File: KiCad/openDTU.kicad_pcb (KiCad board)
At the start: 4 copper layers, 40 x 50 mm, 53 parts, among them J1 USB_C_Receptacle_USB2.0, J2 Conn_Coaxial, J3 Micro_SD_Card, J4 Conn_02x05_Counter_Clockwise, Q1 BC817, Q2 BC817, SW1 SW_Push, SW2 SW_Push, U1 CH340C, U3 ESP32-WROOM-32, U4 nRF24L01P, U5 NCP1117-3.3_SOT223, Y1 Crystal

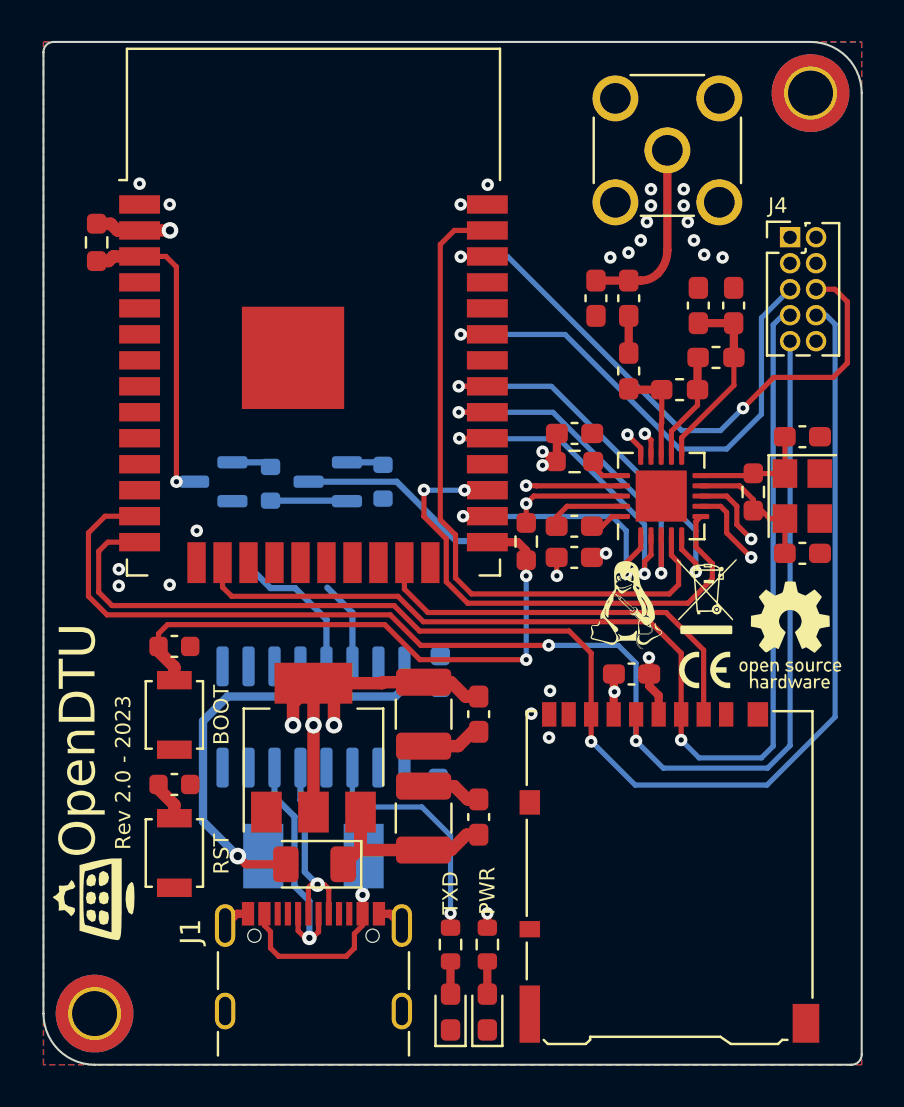
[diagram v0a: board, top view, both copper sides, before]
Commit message: all tracks first time routed
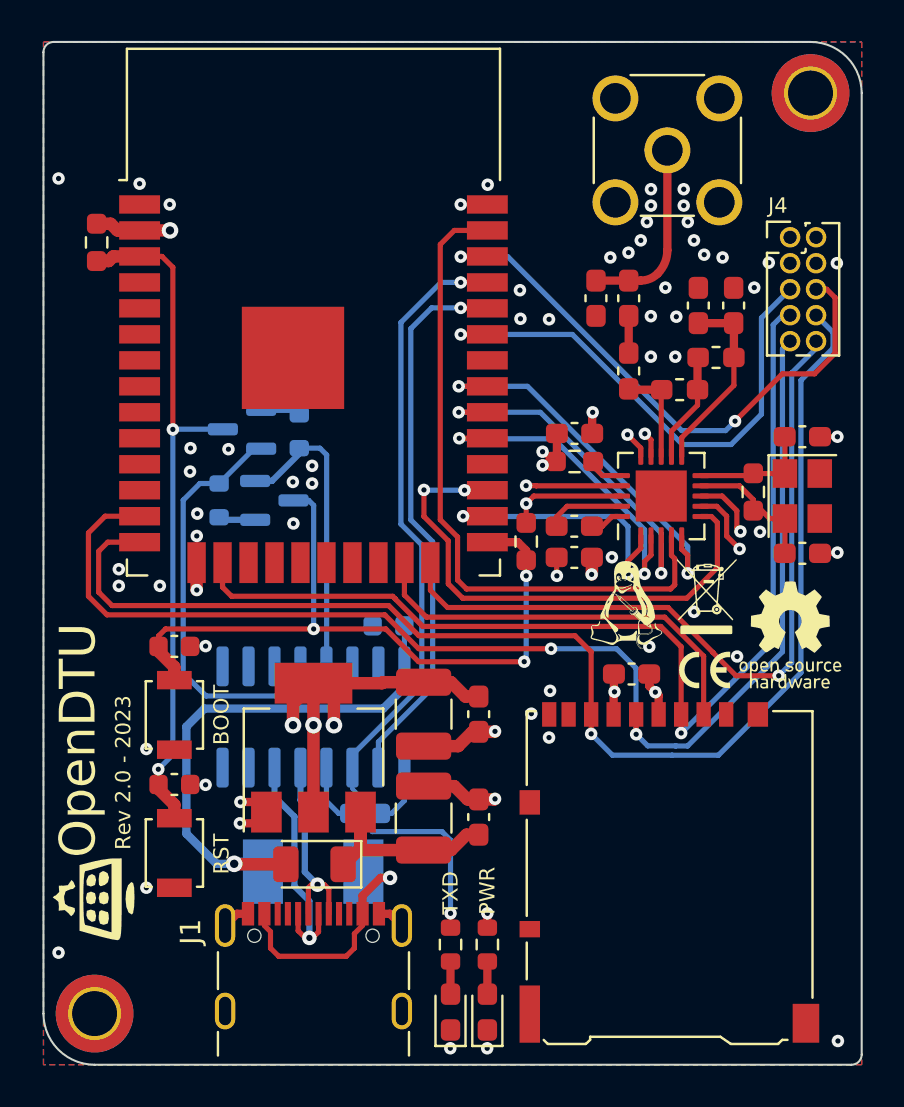
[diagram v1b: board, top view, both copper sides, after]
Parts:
- moved R5 8.06 mm to (134.1, 90.4), turned to -90 degrees
- moved C15 4.37 mm to (141.2, 105.7), turned to 0 degrees
- moved C16 3.39 mm to (142.4, 96.5), turned to 180 degrees
- moved Q1 2.93 mm to (135.2, 86.9)
- moved R4 2.93 mm to (138.0, 87.0)
- moved Q2 2.77 mm to (136.8, 90.4), turned to 0 degrees
- moved F1 0.76 mm to (138.7, 108.6)
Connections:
- J4 pad 10: unconnected-(J4-Pad10) -> /ESP.CS_EXT
- U3 pad 24: unconnected-(U3-Pad24) -> /ESP.CS_EXT
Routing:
- net /ESP.CS_EXT: track 0.00 -> 37.2 mm, vias 0 -> 1
- net /ESP.TXD: track 11.6 -> 40.4 mm, vias 1 -> 2
- net /ESP.RXD: track 0.00 -> 27.2 mm, vias 0 -> 1
- net Net-(Q1-Pad2): track 4.54 -> 23.2 mm
- net /ESP_EN: track 17.5 -> 34.0 mm, vias 1 -> 2
- net GND: track 22.1 -> 33.9 mm, vias 28 -> 69
- net /ESP.SCK_SD: track 67.5 -> 63.0 mm
- net Net-(Q2-Pad2): track 10.8 -> 14.8 mm
- net /ESP.MOSI_SD: track 55.9 -> 51.9 mm
- net /ESP.MISO_SD: track 68.3 -> 64.3 mm
- net Net-(C15-Pad1): track 0.00 -> 3.01 mm
- net /ESP.IO0: track 38.8 -> 35.8 mm, vias 2 -> 3
- net VBUS: track 25.4 -> 27.8 mm
- net +3.3V: track 42.1 -> 40.6 mm
- net /ESP.SCL: track 29.9 -> 28.5 mm
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
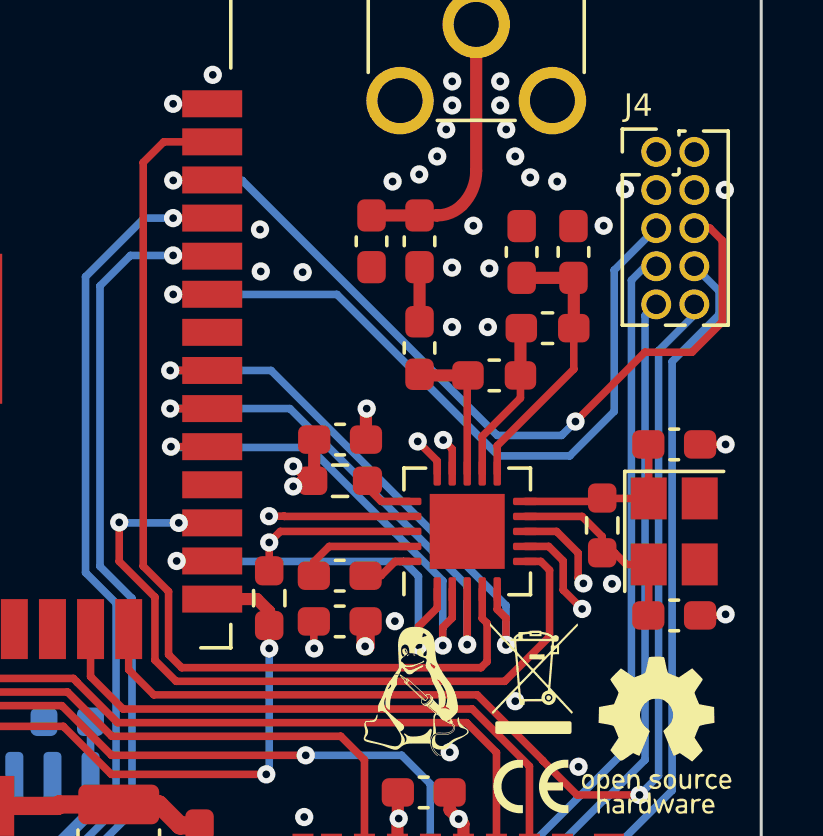
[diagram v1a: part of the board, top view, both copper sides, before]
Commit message: adding Frequency value to crystal an fixing crystal pin/footrpint assignment
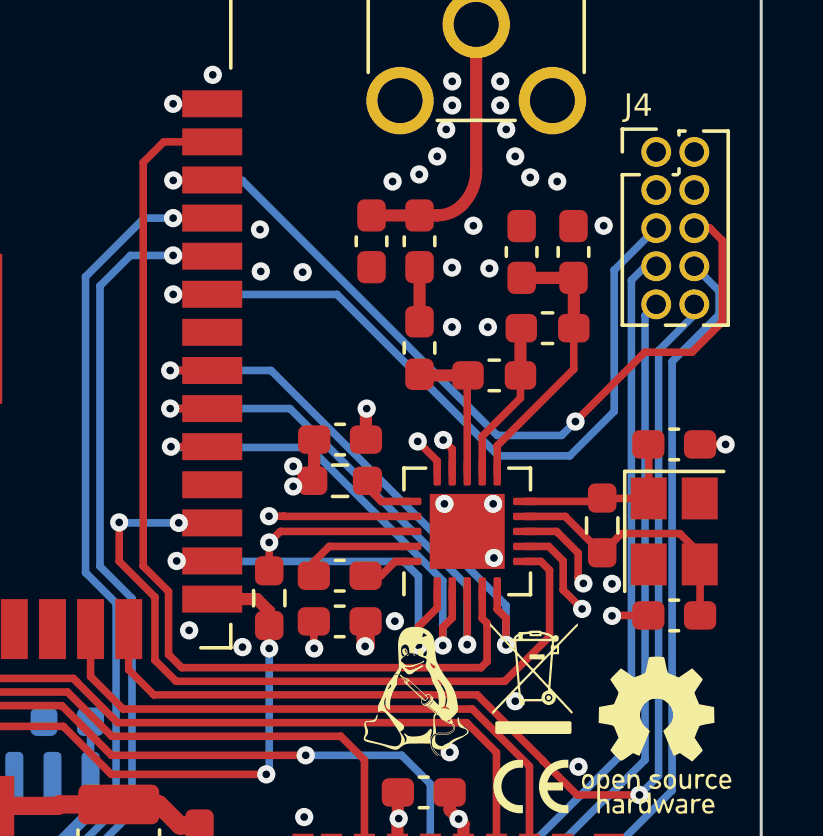
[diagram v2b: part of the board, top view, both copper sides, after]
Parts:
- C15, C16: value 100n -> 100nF
- Y1: value Crystal -> 16 MHz
- turned C5 to 180 degrees
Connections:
- Y1 pad 2: Net-(C5-Pad1) -> (no net)
- Y1 pad 3: (no net) -> Net-(C5-Pad1)
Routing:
- net Net-(C5-Pad1): track 6.80 -> 8.93 mm
- net GND: track 33.9 -> 34.3 mm, vias 69 -> 72

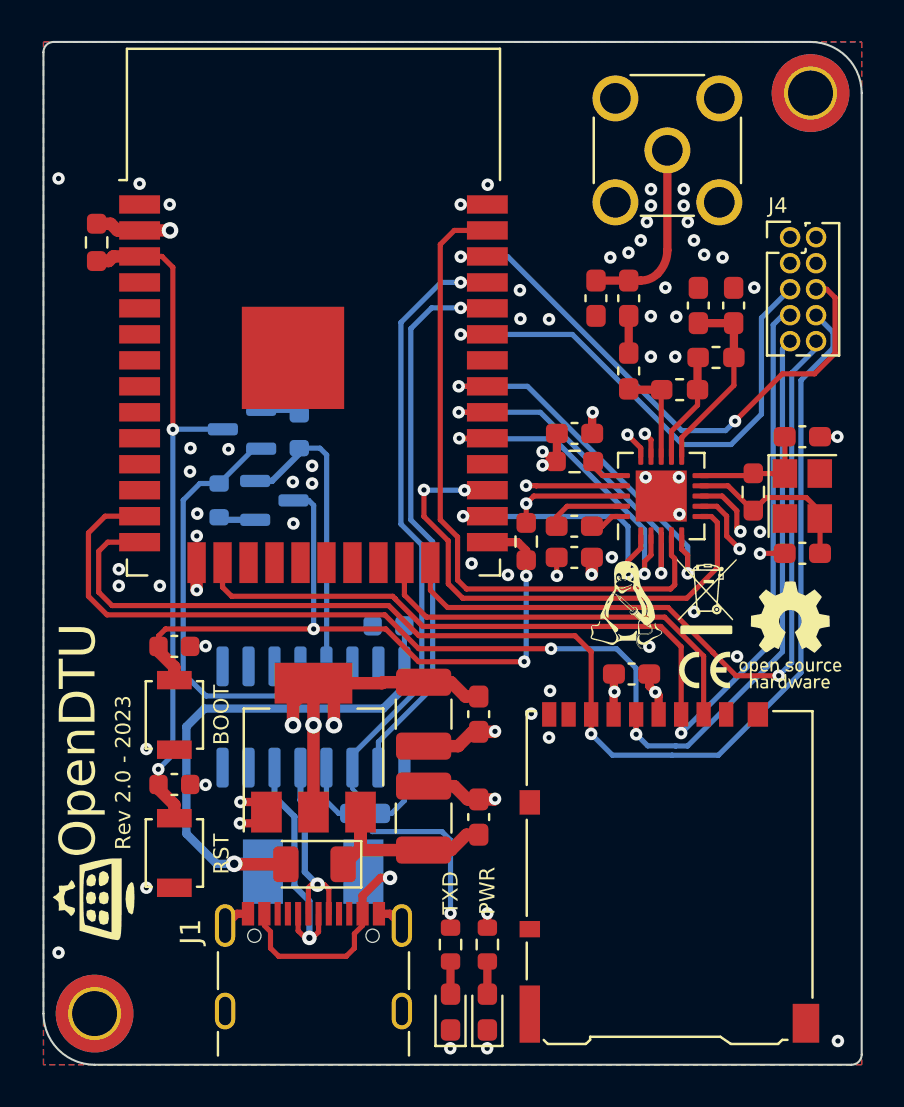
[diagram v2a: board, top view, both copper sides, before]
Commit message: adding 5k1 resistor for A5 and B5 of usb-c
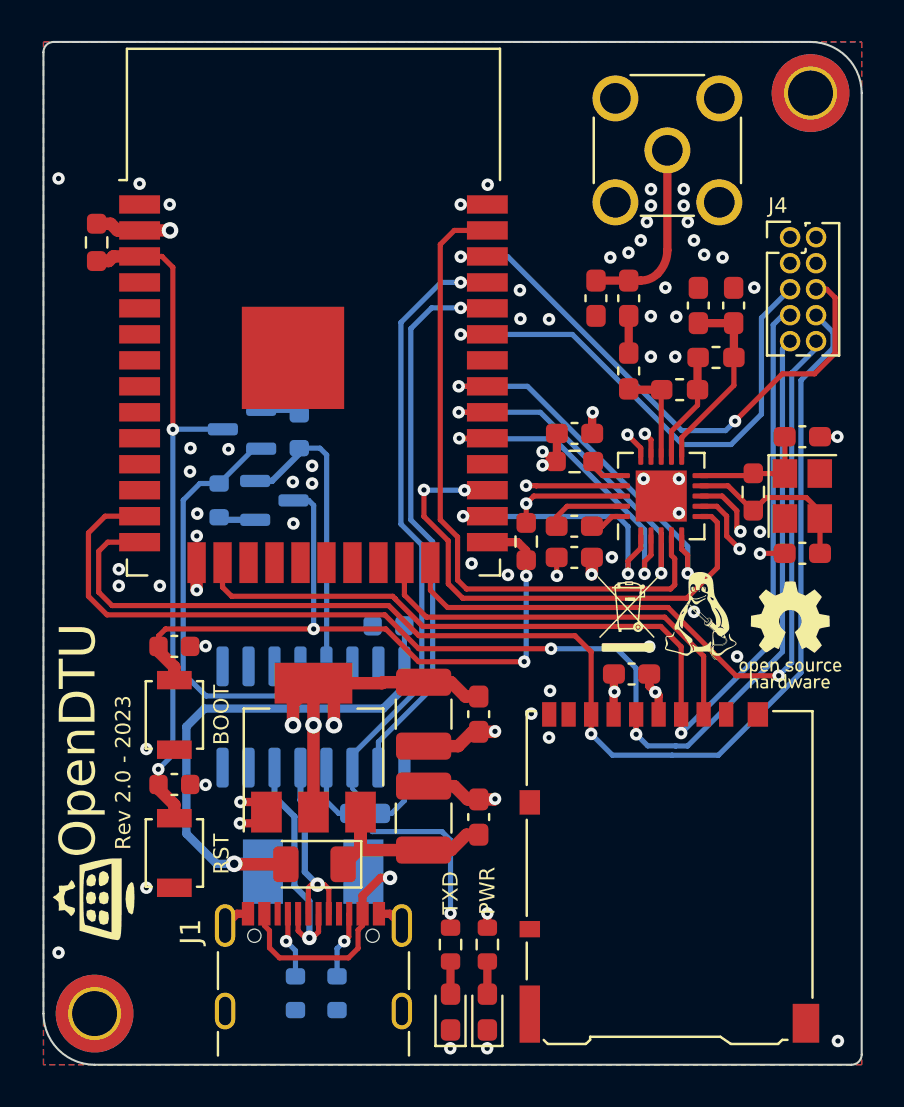
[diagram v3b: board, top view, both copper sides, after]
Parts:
- removed the G*** at (157.8, 98.7)
- added R10: 5k1, Resistor_SMD:R_0603_1608Metric, B.Cu at (137.8, 114.5)
- added R9: 5k1, Resistor_SMD:R_0603_1608Metric, B.Cu at (139.9, 114.5)
- moved G*** 3.94 mm to (154.2, 96.2)
- moved G*** 3.67 mm to (157.6, 95.3)
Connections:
- J1 pad A5: unconnected-(J1-PadA5) -> Net-(J1-PadA5)
- J1 pad B5: unconnected-(J1-PadB5) -> Net-(J1-PadB5)
- U4 pad 21: (no net) -> GND
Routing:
- net Net-(J1-PadB5): track 0.00 -> 3.31 mm, vias 0 -> 1
- net Net-(J1-PadA5): track 0.00 -> 3.28 mm, vias 0 -> 1

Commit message: update color of ESP32 wroom module
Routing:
- net +3.3V: track 40.6 -> 41.2 mm
- net GND: track 34.3 -> 34.9 mm
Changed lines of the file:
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@@
       (layer "F.SilkS" (type "Top Silk Screen") (color "White"))
       (layer "F.Paste" (type "Top Solder Paste"))
-      (layer "F.Mask" (type "Top Solder Mask") (color "Blue") (thickness 0.01))
+      (layer "F.Mask" (type "Top Solder Mask") (color "Black") (thickness 0.01))
       (layer "F.Cu" (type "copper") (thickness 0.035))
       (layer "dielectric 1" (type "prepreg") (thickness 0.14) (material "FR4") (epsilon_r 4.5) (loss_tangent 0.02))
@@
       (layer "dielectric 3" (type "prepreg") (thickness 0.14) (material "FR4") (epsilon_r 4.5) (loss_tangent 0.02))
       (layer "B.Cu" (type "copper") (thickness 0.035))
-      (layer "B.Mask" (type "Bottom Solder Mask") (color "Blue") (thickness 0.01))
+      (layer "B.Mask" (type "Bottom Solder Mask") (color "Black") (thickness 0.01))
       (layer "B.Paste" (type "Bottom Solder Paste"))
       (layer "B.SilkS" (type "Bottom Silk Screen") (color "White"))
@@
       )
     )
-    (model "${KICAD6_3DMODEL_DIR}/RF_Module.3dshapes/ESP32-WROOM-32.wrl"
+    (model "${KICAD6_3DMODEL_DIR}/RF_Module.3dshapes/ESP32-WROOM-32.wrl" hide
       (offset (xyz 0 0 0))
       (scale (xyz 1 1 1))
       (rotate (xyz 0 0 0))
     )
+    (model "${KIPRJMOD}/3D_Models/ESP32-WROOM-32.wrl"
+      (offset (xyz 0 3.048 0))
+      (scale (xyz 1 1 1))
+      (rotate (xyz 0 0 -180))
+    )
   )
   (footprint "Inductor_SMD:L_0603_1608Metric_Pad1.05x0.95mm_HandSolder" (layer "F.Cu")
@@
   (segment (start 155.1125 98.9) (end 155.1125 99.4865) (width 0.4064) (layer "F.Cu") (net 1))
   (segment (start 155.575 99.949) (end 155.575 100.875) (width 0.4064) (layer "F.Cu") (net 1))
+  (segment (start 153.7208 86.6648) (end 154.7 87.644) (width 0.254) (layer "F.Cu") (net 1))
   (segment (start 158.8992 92.152156) (end 158.8992 91.1828) (width 0.254) (layer "F.Cu") (net 1))
-  (segment (start 154.05 87.2) (end 154.7 87.85) (width 0.254) (layer "F.Cu") (net 1))
   (segment (start 128.7875 76.8875) (end 128.1 76.8875) (width 0.6096) (layer "F.Cu") (net 1))
   (segment (start 138.95 99.35) (end 139.7 100.1) (width 0.6096) (layer "F.Cu") (net 1))
   (segment (start 129.115 77.215) (end 128.7875 76.8875) (width 0.6096) (layer "F.Cu") (net 1))
+  (segment (start 154.7 87.644) (end 154.7 88.2625) (width 0.254) (layer "F.Cu") (net 1))
   (segment (start 149.1 90.5687) (end 149.4687 90.2) (width 0.254) (layer "F.Cu") (net 1))
   (segment (start 137.7 101.4) (end 137.7 100.35) (width 0.6096) (layer "F.Cu") (net 1))
@@
   (segment (start 149.1 90.5687) (end 149.1 91.5125) (width 0.254) (layer "F.Cu") (net 1))
   (segment (start 150.0892 88.5108) (end 149.9 88.7) (width 0.254) (layer "F.Cu") (net 1))
-  (segment (start 154.7 87.85) (end 154.7 88.2625) (width 0.254) (layer "F.Cu") (net 1))
   (segment (start 158.8992 91.1828) (end 158.4164 90.7) (width 0.254) (layer "F.Cu") (net 1))
   (segment (start 147.2 111.3) (end 147.2 110.6) (width 0.4064) (layer "F.Cu") (net 1))
@@
   (via (at 138.7 101.4) (size 0.8128) (drill 0.4064) (layers "F.Cu" "B.Cu") (net 1))
   (via (at 155.413 99.787) (size 0.6096) (drill 0.254) (layers "F.Cu" "B.Cu") (net 1))
-  (via (at 154.05 87.2) (size 0.6096) (drill 0.254) (layers "F.Cu" "B.Cu") (net 1))
+  (via (at 153.7208 86.6648) (size 0.6096) (drill 0.254) (layers "F.Cu" "B.Cu") (net 1))
   (segment (start 146.015 91.185) (end 147.2 91.185) (width 0.254) (layer "F.Cu") (net 2))
   (segment (start 154.7 92.75) (end 154.7 92.1375) (width 0.254) (layer "F.Cu") (net 2))
@@
   (segment (start 135.1026 106.1974) (end 135.8526 106.1974) (width 0.4064) (layer "F.Cu") (net 8))
   (segment (start 164.3126 87.3) (end 163.4625 87.3) (width 0.254) (layer "F.Cu") (net 8))
+  (segment (start 155.2 87.1788) (end 155.2 88.2625) (width 0.254) (layer "F.Cu") (net 8))
   (segment (start 152.325 87.1392) (end 152.325 86.1302) (width 0.4064) (layer "F.Cu") (net 8))
   (segment (start 153.375 100.875) (end 153.375 99.8122) (width 0.4064) (layer "F.Cu") (net 8))
   (segment (start 132.985 94.7834) (end 132.9944 94.7928) (width 0.6096) (layer "F.Cu") (net 8))
   (segment (start 152.824 91.676) (end 152.3125 91.676) (width 0.254) (layer "F.Cu") (net 8))
-  (segment (start 154.9 87.153603) (end 155.2 87.453603) (width 0.254) (layer "F.Cu") (net 8))
   (segment (start 152.3125 94.0167) (end 152.2984 94.0308) (width 0.6096) (layer "F.Cu") (net 8))
   (segment (start 161.7375 93) (end 160.5428 93) (width 0.254) (layer "F.Cu") (net 8))
@@
   (segment (start 145.5807 104.3807) (end 144.0848 104.3807) (width 0.6096) (layer "F.Cu") (net 8))
   (segment (start 153.3 91.2) (end 152.824 91.676) (width 0.254) (layer "F.Cu") (net 8))
+  (segment (start 154.686 86.6648) (end 155.2 87.1788) (width 0.254) (layer "F.Cu") (net 8))
   (segment (start 159.572422 91.932584) (end 159.398 91.758162) (width 0.254) (layer "F.Cu") (net 8))
-  (segment (start 155.2 87.453603) (end 155.2 88.2625) (width 0.254) (layer "F.Cu") (net 8))
   (segment (start 142.445 110.62) (end 143.02 111.195) (width 0.4064) (layer "F.Cu") (net 8))
   (segment (start 146.7772 105.0299) (end 146.2299 105.0299) (width 0.6096) (layer "F.Cu") (net 8))
@@
   (via (at 137.6934 89.5096) (size 0.6096) (drill 0.254) (layers "F.Cu" "B.Cu") (free) (net 8))
   (via (at 130.5306 109.347) (size 0.6096) (drill 0.254) (layers "F.Cu" "B.Cu") (free) (net 8))
-  (via (at 154.9 87.153603) (size 0.6096) (drill 0.254) (layers "F.Cu" "B.Cu") (net 8))
+  (via (at 154.686 86.6648) (size 0.6096) (drill 0.254) (layers "F.Cu" "B.Cu") (net 8))
   (via (at 149.352 100.838) (size 0.6096) (drill 0.254) (layers "F.Cu" "B.Cu") (free) (net 8))
   (via (at 150.2664 99.7204) (size 0.6096) (drill 0.254) (layers "F.Cu" "B.Cu") (free) (net 8))
